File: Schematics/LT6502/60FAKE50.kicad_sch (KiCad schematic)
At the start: 17 parts, among them J6 USB_C_Receptacle_USB2.0_16P, J7 Conn_01x02, Q2 IRLML6402, U10 FT245RNL

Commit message: Tweaks to Schematics
Shrunk main PCB
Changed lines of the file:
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@@
 					(size 1.27 1.27)
 				)
+				(hide yes)
 			)
 		)

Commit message: Further work on Schematics, All parts placed on PCB
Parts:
- C39, C40: footprint Capacitor_SMD:C_0603_1608Metric_Pad1.08x0.95mm_HandSolder -> Capacitor_SMD:C_0603_1608Metric
- R70, R71, R72, R73, R74: footprint Resistor_SMD:R_0603_1608Metric_Pad0.98x0.95mm_HandSolder -> Resistor_SMD:R_0402_1005Metric
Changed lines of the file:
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@@
 			)
 		)
-		(property "Footprint" "Resistor_SMD:R_0603_1608Metric_Pad0.98x0.95mm_HandSolder"
+		(property "Footprint" "Resistor_SMD:R_0402_1005Metric"
 			(at 117.348 60.96 90)
 			(effects
@@
 			)
 		)
-		(property "Footprint" "Resistor_SMD:R_0603_1608Metric_Pad0.98x0.95mm_HandSolder"
+		(property "Footprint" "Resistor_SMD:R_0402_1005Metric"
 			(at 229.108 101.6 90)
 			(effects
@@
 			)
 		)
-		(property "Footprint" "Capacitor_SMD:C_0603_1608Metric_Pad1.08x0.95mm_HandSolder"
+		(property "Footprint" "Capacitor_SMD:C_0603_1608Metric"
 			(at 155.9052 116.84 0)
 			(effects
@@
 			)
 		)
-		(property "Footprint" "Resistor_SMD:R_0603_1608Metric_Pad0.98x0.95mm_HandSolder"
+		(property "Footprint" "Resistor_SMD:R_0402_1005Metric"
 			(at 107.188 60.96 90)
 			(effects
@@
 			)
 		)
-		(property "Footprint" "Resistor_SMD:R_0603_1608Metric_Pad0.98x0.95mm_HandSolder"
+		(property "Footprint" "Resistor_SMD:R_0402_1005Metric"
 			(at 148.59 88.392 90)
 			(effects
@@
 			)
 		)
-		(property "Footprint" "Resistor_SMD:R_0603_1608Metric_Pad0.98x0.95mm_HandSolder"
+		(property "Footprint" "Resistor_SMD:R_0402_1005Metric"
 			(at 221.488 93.98 90)
 			(effects
@@
 			)
 		)
-		(property "Footprint" "Capacitor_SMD:C_0603_1608Metric_Pad1.08x0.95mm_HandSolder"
+		(property "Footprint" "Capacitor_SMD:C_0603_1608Metric"
 			(at 239.7252 95.25 0)
 			(effects

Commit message: Updated main board and started keybed
main board a bit wider due to keybed width
created keybed, begun routing
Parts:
- Q2: Mouser Part Number (none) -> 942-IRLML6402TRPBF
- R70, R71: now not fitted
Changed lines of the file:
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@@
 		(in_bom yes)
 		(on_board yes)
-		(dnp no)
+		(dnp yes)
 		(property "Reference" "R71"
 			(at 117.856 60.96 90)
@@
 		(in_bom yes)
 		(on_board yes)
-		(dnp no)
+		(dnp yes)
 		(property "Reference" "R70"
 			(at 107.442 60.96 90)
@@
 			(at 227.33 90.17 0)
 			(effects
+				(font
+					(size 1.27 1.27)
+				)
+				(hide yes)
+			)
+		)
+		(property "Mouser Part Number" "942-IRLML6402TRPBF"
+			(at 227.33 90.17 0)
+			(effects

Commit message: Updated BoMs ordered PCBs
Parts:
- C41: LCSC C96123 -> C22367835
- FB1, J6, J7: now not fitted
- R72: LCSC DNF -> C25744
- U10: LCSC C6558294 -> DNF; now not fitted
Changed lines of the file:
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@@
 		(in_bom yes)
 		(on_board yes)
-		(dnp no)
+		(dnp yes)
 		(fields_autoplaced yes)
 		(property "Reference" "J6"
@@
 		(in_bom yes)
 		(on_board yes)
-		(dnp no)
+		(dnp yes)
 		(fields_autoplaced yes)
 		(property "Reference" "J7"
@@
 		(in_bom yes)
 		(on_board yes)
-		(dnp no)
+		(dnp yes)
 		(fields_autoplaced yes)
 		(property "Reference" "U10"
@@
 			)
 		)
-		(property "LCSC" "C6558294"
+		(property "LCSC" "DNF"
 			(at 180.34 87.63 0)
 			(effects
@@
 			)
 		)
-		(property "LCSC" "C96123"
+		(property "LCSC" "C22367835"
 			(at 248.92 53.975 0)
 			(effects
@@
 			)
 		)
-		(property "LCSC" "DNF"
+		(property "LCSC" "C25744"
 			(at 148.59 90.17 90)
 			(effects
@@
 		(in_bom yes)
 		(on_board yes)
-		(dnp no)
+		(dnp yes)
 		(fields_autoplaced yes)
 		(property "Reference" "FB1"

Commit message: Auto stash before merge of "main" and "origin/main"
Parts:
- FB1, J6, U10: now fitted
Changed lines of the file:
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@@
 		(in_bom yes)
 		(on_board yes)
-		(dnp yes)
+		(dnp no)
 		(fields_autoplaced yes)
 		(property "Reference" "J6"
@@
 		(in_bom yes)
 		(on_board yes)
-		(dnp yes)
+		(dnp no)
 		(fields_autoplaced yes)
 		(property "Reference" "U10"
@@
 		(in_bom yes)
 		(on_board yes)
-		(dnp yes)
+		(dnp no)
 		(fields_autoplaced yes)
 		(property "Reference" "FB1"

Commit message: LED value change, added fix for FTDI power
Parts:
- added D1, D14: D_Schottky, symbol Device:D_Schottky
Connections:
- net +5V: now also D14.2 (A)
- net VUSB: now also D1.1 (K), D14.1 (K); no longer FB1.1
- new net: D1.2 (A), FB1.1
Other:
- note added: "D1 and D14 are to ensure the FTDI245 has power when not connected to USB which stops the system from booting"
- moved on the sheet: C38, FB1

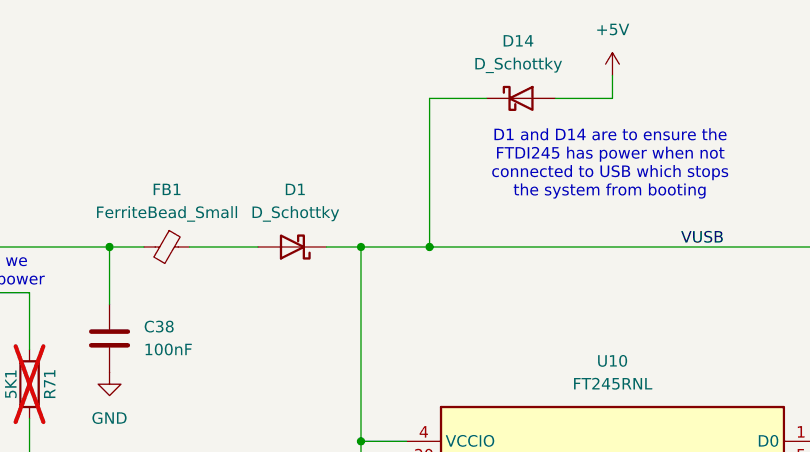
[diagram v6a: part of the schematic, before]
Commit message: PCB/Schematic edits
moved speaker hole a little
made nRES resistor for display no fit (this upsets them for some reason)
Added diodes to ensure USB Console chip is powered when nothing attached (this causes issues with booting.
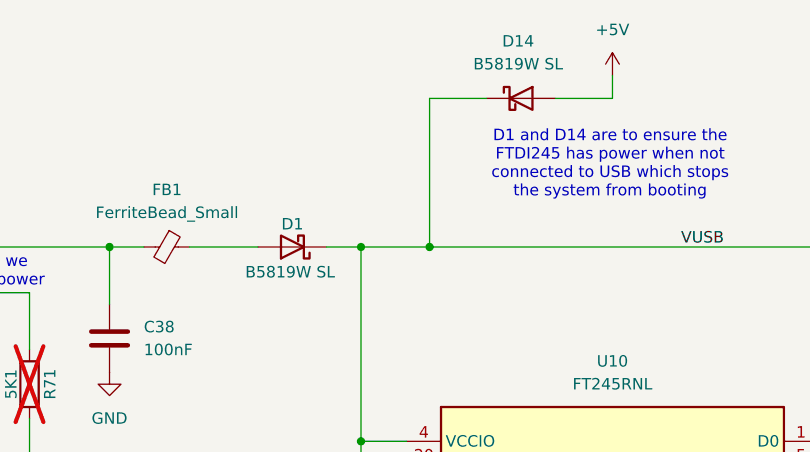
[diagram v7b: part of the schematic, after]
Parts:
- D1, D14: value D_Schottky -> B5819W SL; footprint (none) -> Diode_SMD:D_SOD-123; LCSC (none) -> C8598
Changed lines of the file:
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@@
 			)
 		)
-		(property "Value" "D_Schottky"
+		(property "Value" "B5819W SL"
 			(at 169.8625 25.4 0)
 			(effects
@@
 			)
 		)
-		(property "Footprint" ""
+		(property "Footprint" "Diode_SMD:D_SOD-123"
 			(at 170.18 29.21 0)
 			(effects
@@
 		)
 		(property "Description" "Schottky diode"
+			(at 170.18 29.21 0)
+			(effects
+				(font
+					(size 1.27 1.27)
+				)
+				(hide yes)
+			)
+		)
+		(property "LCSC" "C8598"
 			(at 170.18 29.21 0)
 			(effects
@@
 		(on_board yes)
 		(dnp no)
-		(fields_autoplaced yes)
 		(property "Reference" "D1"
-			(at 145.0975 39.37 0)
-			(effects
-				(font
-					(size 1.27 1.27)
-				)
-			)
-		)
-		(property "Value" "D_Schottky"
-			(at 145.0975 41.91 0)
-			(effects
-				(font
-					(size 1.27 1.27)
-				)
-			)
-		)
-		(property "Footprint" ""
+			(at 144.78 43.18 0)
+			(effects
+				(font
+					(size 1.27 1.27)
+				)
+			)
+		)
+		(property "Value" "B5819W SL"
+			(at 144.526 48.514 0)
+			(effects
+				(font
+					(size 1.27 1.27)
+				)
+			)
+		)
+		(property "Footprint" "Diode_SMD:D_SOD-123"
 			(at 144.78 45.72 0)
 			(effects
@@
 			(at 144.78 45.72 0)
 			(effects
+				(font
+					(size 1.27 1.27)
+				)
+				(hide yes)
+			)
+		)
+		(property "LCSC" "C8598"
+			(at 144.78 45.72 0)
+			(effects
